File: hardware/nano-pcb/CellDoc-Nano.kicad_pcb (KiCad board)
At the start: 2 copper layers, 95 x 76 mm, 27 parts, among them J1 Lastwiderstand 3 Ohm, J2 DS18B20 Zelle, J3 DS18B20 Last opt., J4 OLED opt., J5 QR GM861S opt., Q1 AO3400, Q2 AO3401, Q3 AO3400, Q4 AO3400 opt., U1 ESP32-C3 SuperMini, U2 INA226 (Shunt R010), U3 TP4056 USB-C

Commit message: Nano-Platine neu erzeugt (Thermals, R1)
Co-Authored-By: Claude Opus 5.5 <noreply@anthropic.com>
Claude-Session: https://claude.ai/code/session_01WtJ5FLprrJxW2qKdxjRQsn
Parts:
- moved R1 2.00 mm to (3.50, 29.0)
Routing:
- net CHG: track 40.3 -> 52.8 mm
- net SCL: track 69.5 -> 81.8 mm
- net GND: track 220.0 -> 228.3 mm
- net SCAN_RX: track 45.2 -> 52.3 mm, vias 1 -> 2
- net BUZZER: track 88.0 -> 81.8 mm, vias 2 -> 0
- net Q2_G: track 28.3 -> 23.7 mm, vias 1 -> 2
- net ONEWIRE: track 42.0 -> 45.0 mm, vias 1 -> 0
- net +3V3: track 89.7 -> 92.2 mm, vias 0 -> 1
- net LOAD_PWM: track 62.1 -> 60.6 mm
- net SDA: track 71.5 -> 72.6 mm, vias 0 -> 2

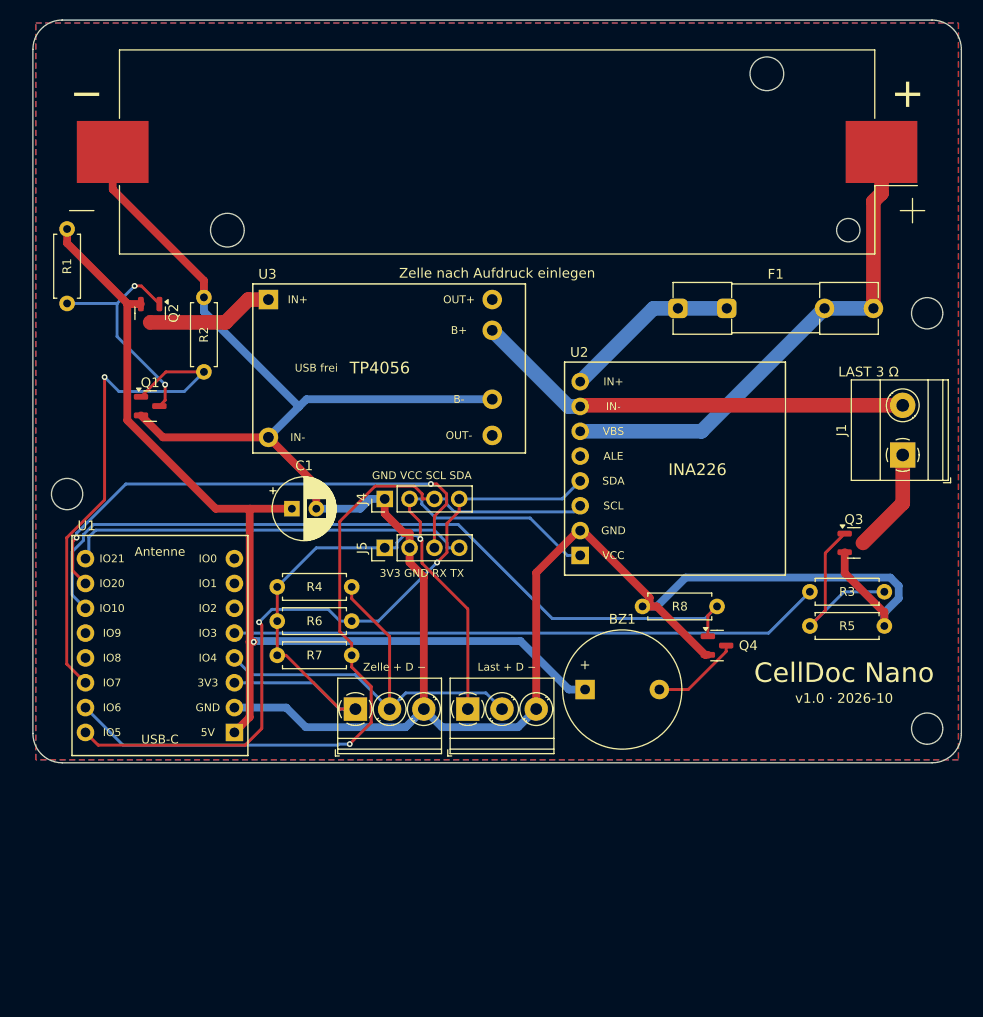
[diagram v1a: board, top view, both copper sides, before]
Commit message: Nano-Platine: alle GND-Pads voll an Flaeche
Co-Authored-By: Claude Opus 5.5 <noreply@anthropic.com>
Claude-Session: https://claude.ai/code/session_01WtJ5FLprrJxW2qKdxjRQsn
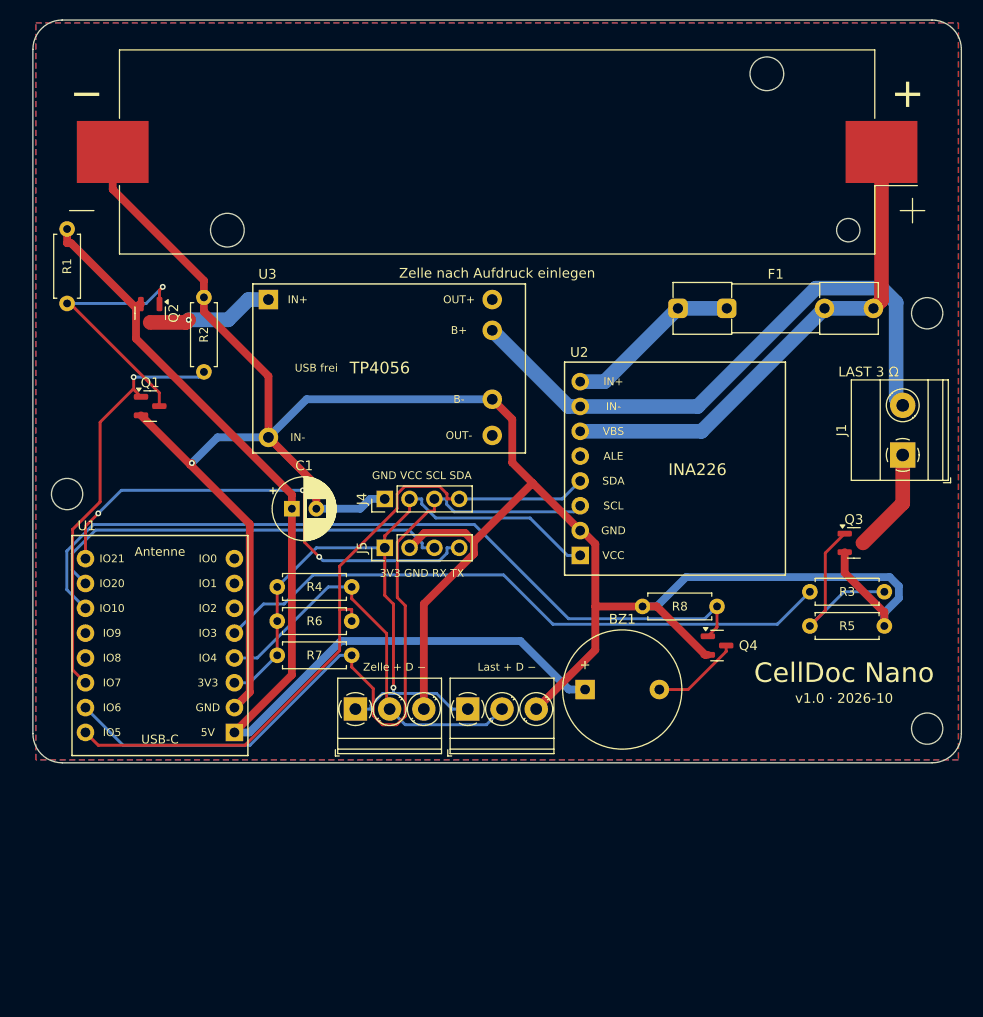
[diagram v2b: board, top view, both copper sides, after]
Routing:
- net GND: track 228.3 -> 250.8 mm, vias 0 -> 1
- net CELL: track 45.3 -> 61.0 mm
- net +3V3: track 92.2 -> 79.8 mm
- net CHG: track 52.8 -> 42.9 mm
- net SCAN_RX: track 52.3 -> 42.7 mm, vias 2 -> 0
- net SCAN_TX: track 41.6 -> 49.9 mm, vias 0 -> 3
- net LOAD_PWM: track 60.6 -> 64.8 mm
- net Q2_G: track 23.7 -> 27.0 mm, vias 2 -> 1
- net ONEWIRE: track 45.0 -> 41.9 mm
- net SCL: track 81.8 -> 84.3 mm, vias 1 -> 0
- net +5V: track 104.0 -> 106.2 mm, vias 1 -> 0
- net SDA: track 72.6 -> 72.1 mm, vias 2 -> 0
- net TP_IN: vias 0 -> 1

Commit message: Nano-Platine v1.1: Halter mit Kabeln, Sicherungshalter und 50-W-Lastwiderstand direkt auf der Platine
- 95 x 100 mm, Lastwiderstand mit 2 x M3 verschraubt, Loetfahnen auf Loetaugen
- 18650-Halter mit M3 mittig, Kabel in Loetaugen
- Kabel-Sicherungshalter 5x20 auf Loetaugen
- C3 mit USB-C an der linken Kante, Summer bleibt bestueckbar

Co-Authored-By: Claude Opus 5.5 <noreply@anthropic.com>
Claude-Session: https://claude.ai/code/session_01WtJ5FLprrJxW2qKdxjRQsn
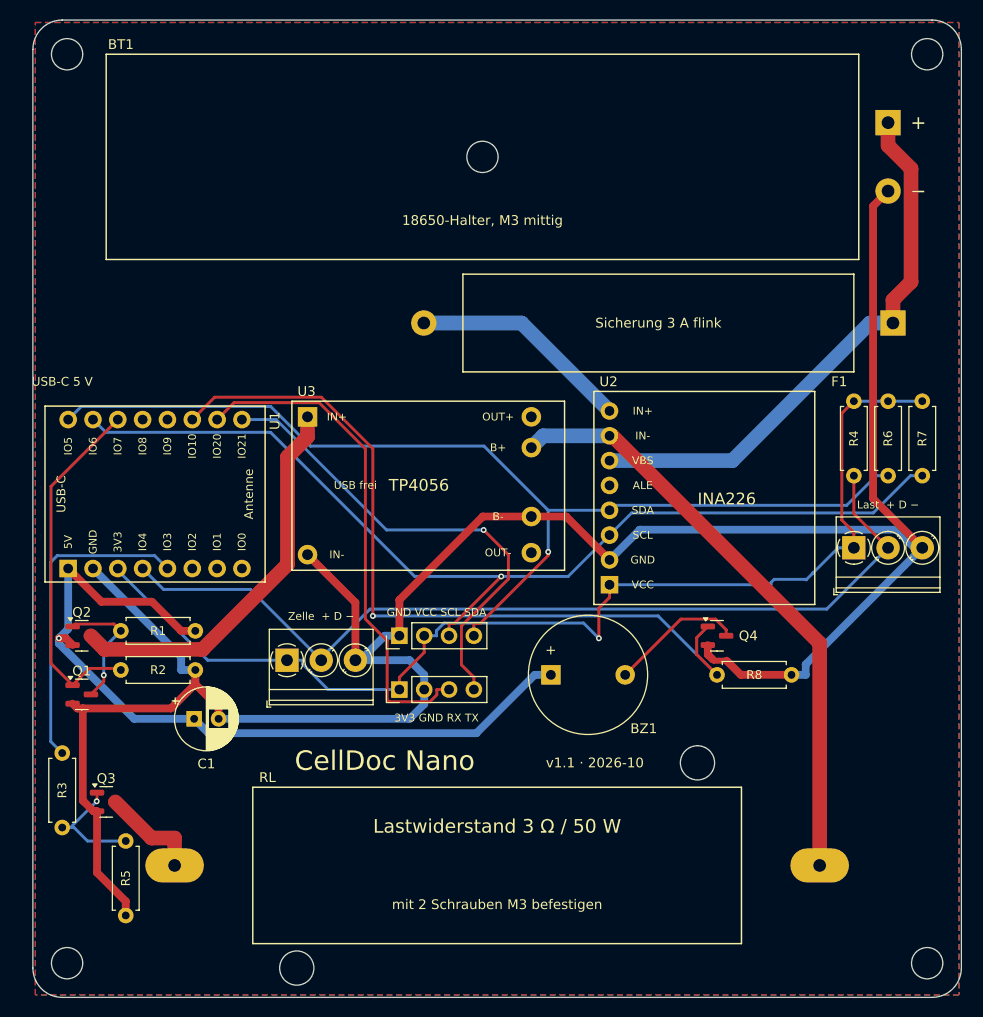
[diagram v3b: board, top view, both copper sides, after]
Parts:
- removed J1: Lastwiderstand 3 Ohm, TerminalBlock_Phoenix_MKDS-1,5-2-5.08_1x02_P5.08mm_Horizontal
- added H4: MountingHole_3.2mm_M3, MountingHole_3.2mm_M3, F.Cu at (91.5, 96.5)
- added RL: 3R 50W, CellDoc:Lastwiderstand_50W_Alu, F.Cu at (47.5, 86.5)
- BT1: value 18650 Keystone 1042 -> 18650-Halter; footprint BatteryHolder_Keystone_1042_1x18650 -> CellDoc:18650_Halter_Kabel
- BZ1: value Summer 5V opt. -> Summer 5V
- F1: footprint Fuseholder_Clip-5x20mm_Littelfuse_111_Inline_P20.00x5.00mm_D1.05mm_Horizontal -> CellDoc:Sicherungshalter_Kabel_5x20
- Q4: value AO3400 opt. -> AO3400
- R8: value 10k opt. -> 10k
- moved H3 91.2 mm to (3.50, 96.5)
- moved Q3 81.0 mm to (7.50, 80.0)
- moved R3 78.3 mm to (3.00, 75.0), turned to -90 degrees
- moved R5 73.4 mm to (9.50, 84.0), turned to -90 degrees
- moved R7 70.9 mm to (91.0, 39.0), turned to -90 degrees
- moved R6 66.4 mm to (87.5, 39.0), turned to -90 degrees
- moved R4 62.0 mm to (84.0, 39.0), turned to -90 degrees
- moved H1 45.0 mm to (3.50, 3.50)
- moved J3 42.8 mm to (84.0, 54.0)
- moved R1 33.9 mm to (9.00, 62.5), turned to 0 degrees
- moved Q2 33.7 mm to (5.00, 63.0), turned to 0 degrees
- moved R2 31.7 mm to (9.00, 66.5), turned to 0 degrees
- moved Q1 30.3 mm to (5.00, 69.0)
- moved H2 26.5 mm to (91.5, 3.50)
- moved C1 23.7 mm to (16.5, 71.5)
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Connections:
- F1 pad 1: BAT_F -> BAT+
- F1 pad 2: BAT+ -> BAT_F
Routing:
- net ONEWIRE: track 41.9 -> 93.9 mm
- net +3V3: track 79.8 -> 115.9 mm
- net SDA: track 72.1 -> 106.7 mm, vias 0 -> 1
- net LOAD_PWM: track 64.8 -> 32.8 mm
- net TP_IN: track 13.1 -> 40.2 mm, vias 1 -> 0
- net +5V: track 106.2 -> 82.0 mm, vias 0 -> 1
- net SCL: track 84.3 -> 104.4 mm, vias 0 -> 1
- net Q2_G: track 27.0 -> 13.1 mm
- net SCAN_RX: track 42.7 -> 51.7 mm
- net GND: track 250.8 -> 242.4 mm, vias 1 -> 0
- net LOAD_G: track 20.0 -> 11.8 mm, vias 0 -> 1
- net CHG: track 42.9 -> 36.6 mm, vias 1 -> 0
- net BAT+: track 51.6 -> 57.1 mm
- net BZ_N: track 9.06 -> 13.8 mm
- net BAT_F: track 18.1 -> 22.7 mm
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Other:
- board size 95 x 76 mm -> 95 x 100 mm
- board text added: "USB-C 5 V"
- board text added: "v1.1 · 2026-10"
- board text removed: "+"
- board text removed: "LAST 3 Ω"
- board text removed: "Zelle nach Aufdruck einlegen"
- board text removed: "v1.0 · 2026-10"
- board text removed: "−"
